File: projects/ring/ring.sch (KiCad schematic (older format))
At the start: 4 parts, among them U1 STM32WB55CEU6TR, Y1 NX1612SA-32.000MHZ-CHP-CIS-3

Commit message: layout and schem changes
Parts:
- removed E1: NN02-101, step-footprints:XCVR_NN02-101, symbol step:NN02-101
- added C1, C10, C11, C2, C5, C6, C8: C_100nF, Capacitor_SMD:C_0402_1005Metric, symbol step:C_100nF
- added C7, C9: C_4.7uF, Capacitor_SMD:C_01005_0402Metric, symbol step:C_4.7uF
- added L1: L_10uH_LQM21FN100M70L, Inductor_SMD:L_0805_2012Metric, symbol step:L_10uH_LQM21FN100M70L
- added L2: L_10nH_LQG15WZ10NJ02D, Inductor_SMD:L_0402_1005Metric, symbol step:L_10nH_LQG15WZ10NJ02D
- added TP1, TP2, TP3, TP4, TP5: Test_Point_SMD, footprints:Test_Point_SMD, symbol step:Test_Point_SMD
- added U2: LSM6DSO32TR, step-footprints:LSM6DSO32TR, symbol step:LSM6DSO32TR
- added U3: ANT016008LCS2442MA2, step-footprints:ANT016008LCS2442MA2, symbol step:ANT016008LCS2442MA2
- added U4: BQ297xy, Package_SON:WSON-6_1.5x1.5mm_P0.5mm, symbol Battery_Management:BQ297xy
- Y1: footprint OSCSC105P160X120X35-4N -> step-footprints:OSCSC105P160X120X35-4N
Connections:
- net labels added: +BATT, BOOT0, CS, LSM_INT1, LSM_INT2, MISO, MOSI, SCK, SWCLK, SWDIO, rad_plane
- wire segments 11 -> 45
- no-connect marks 0 -> 6
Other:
- note added: "Accelerometer"
- note added: "Can be connected to any STM GPIO \nand used to wake from sleep mode \nvia the EXTI Interrupt"
- note added: "Inductors for \nOn-Die SMPS"
- note added: "Integrated Passive Device \nMatching, PI, LP Filter"
- note added: "SMD Chip Antenna"
- note added: "STM smps"
- note added: "fets @sam"
- note added: "power net"
- note added: "should be vreg"
- moved on the sheet: Y1

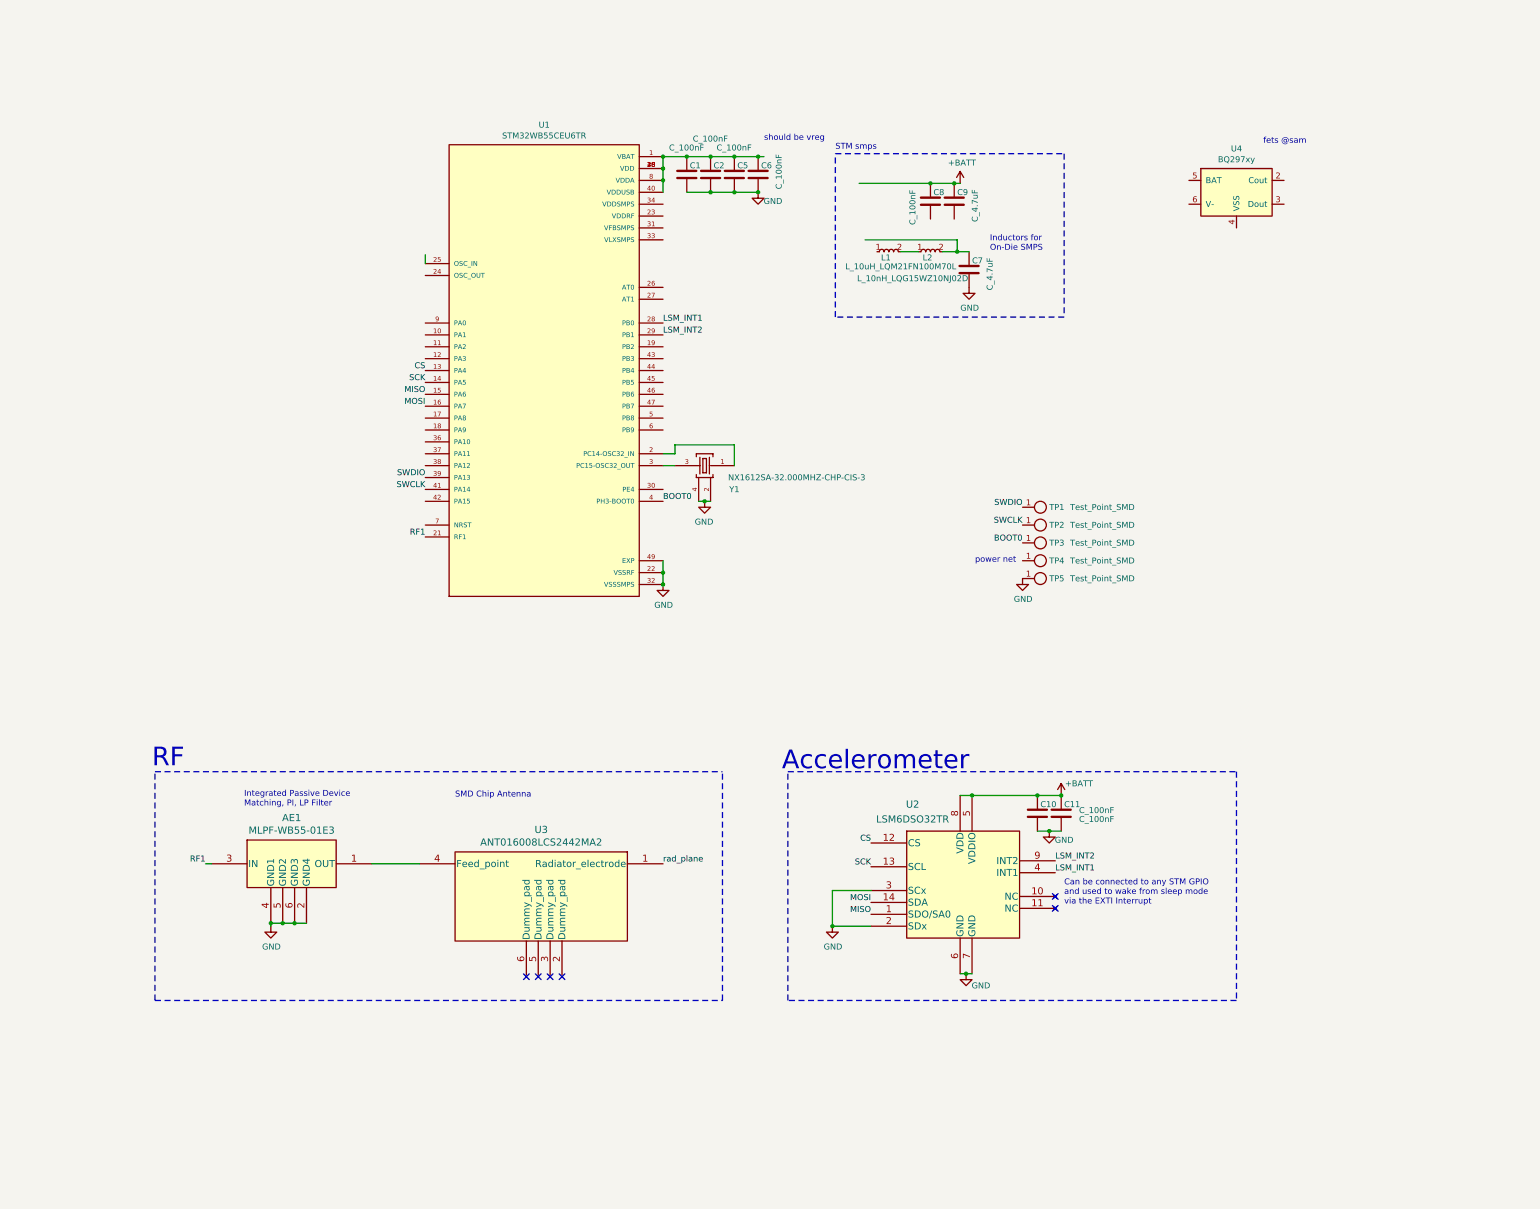
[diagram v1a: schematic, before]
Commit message: ring hardware schem & layout updates
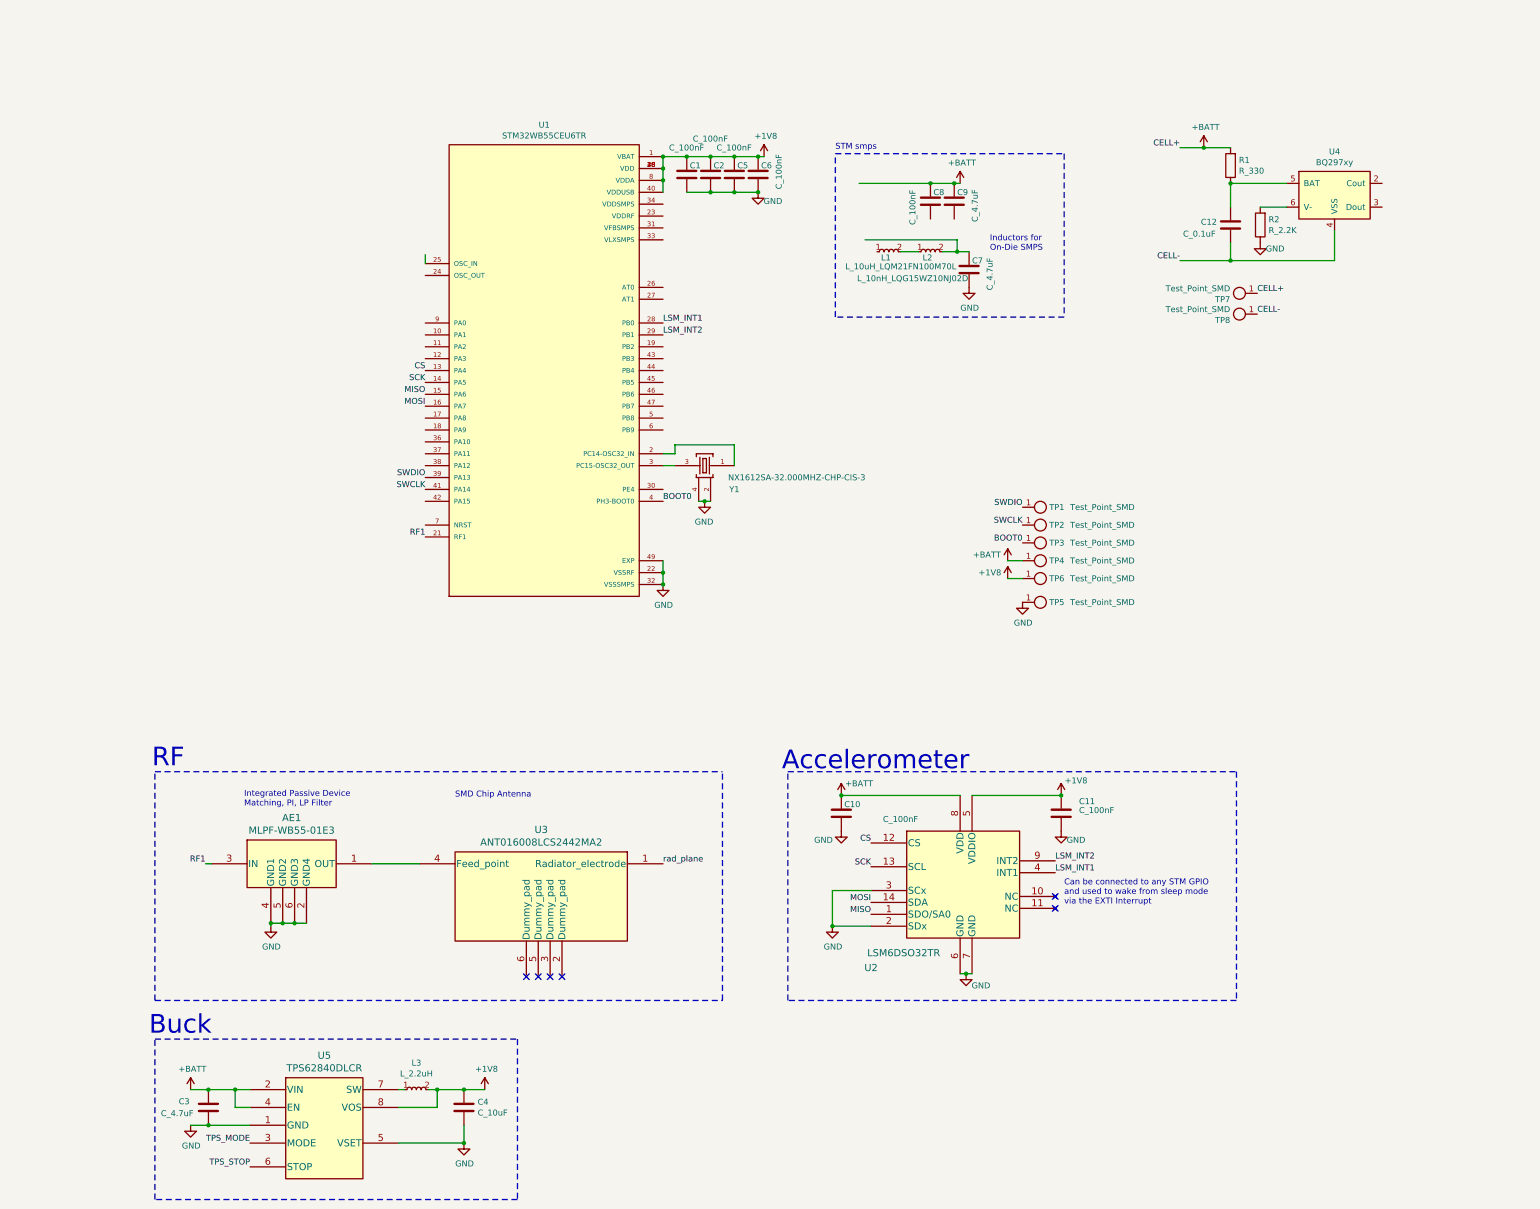
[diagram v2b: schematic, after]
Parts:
- added C12: C_0.1uF, footprints:C_0805_OEM, symbol step:C_0.1uF
- added C3: C_4.7uF, Capacitor_SMD:C_0402_1005Metric, symbol step:C_4.7uF
- added C4: C_10uF, Capacitor_SMD:C_0402_1005Metric, symbol step:C_10uF
- added L3: L_2.2uH, Inductor_SMD:L_0805_2012Metric_Pad1.05x1.20mm_HandSolder, symbol step:L_2.2uH
- added R1: R_330, Resistor_SMD:R_0402_1005Metric, symbol step:R_330
- added R2: R_2.2K, Resistor_SMD:R_0402_1005Metric, symbol step:R_2.2K
- added TP6: Test_Point_SMD, TestPoint:TestPoint_Pad_1.0x1.0mm, symbol step:Test_Point_SMD
- added TP7, TP8: Test_Point_SMD, footprints:Test_Point_SMD, symbol step:Test_Point_SMD
- added U5: TPS62840DLCR, step-footprints:TPS62840DLCR, symbol step:TPS62840DLCR
- C7, C9: footprint Capacitor_SMD:C_01005_0402Metric -> Capacitor_SMD:C_0402_1005Metric
- TP1, TP2, TP3, TP4, TP5: footprint footprints:Test_Point_SMD -> TestPoint:TestPoint_Pad_1.0x1.0mm
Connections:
- net labels added: +1V8, CELL+, CELL-, TPS_MODE, TPS_STOP
- wire segments 45 -> 68
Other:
- note added: "Buck"
- note removed: "fets @sam"
- note removed: "power net"
- note removed: "should be vreg"
- moved on the sheet: C10, TP5, U4

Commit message: nearly complete first pass schem, RF ready for review
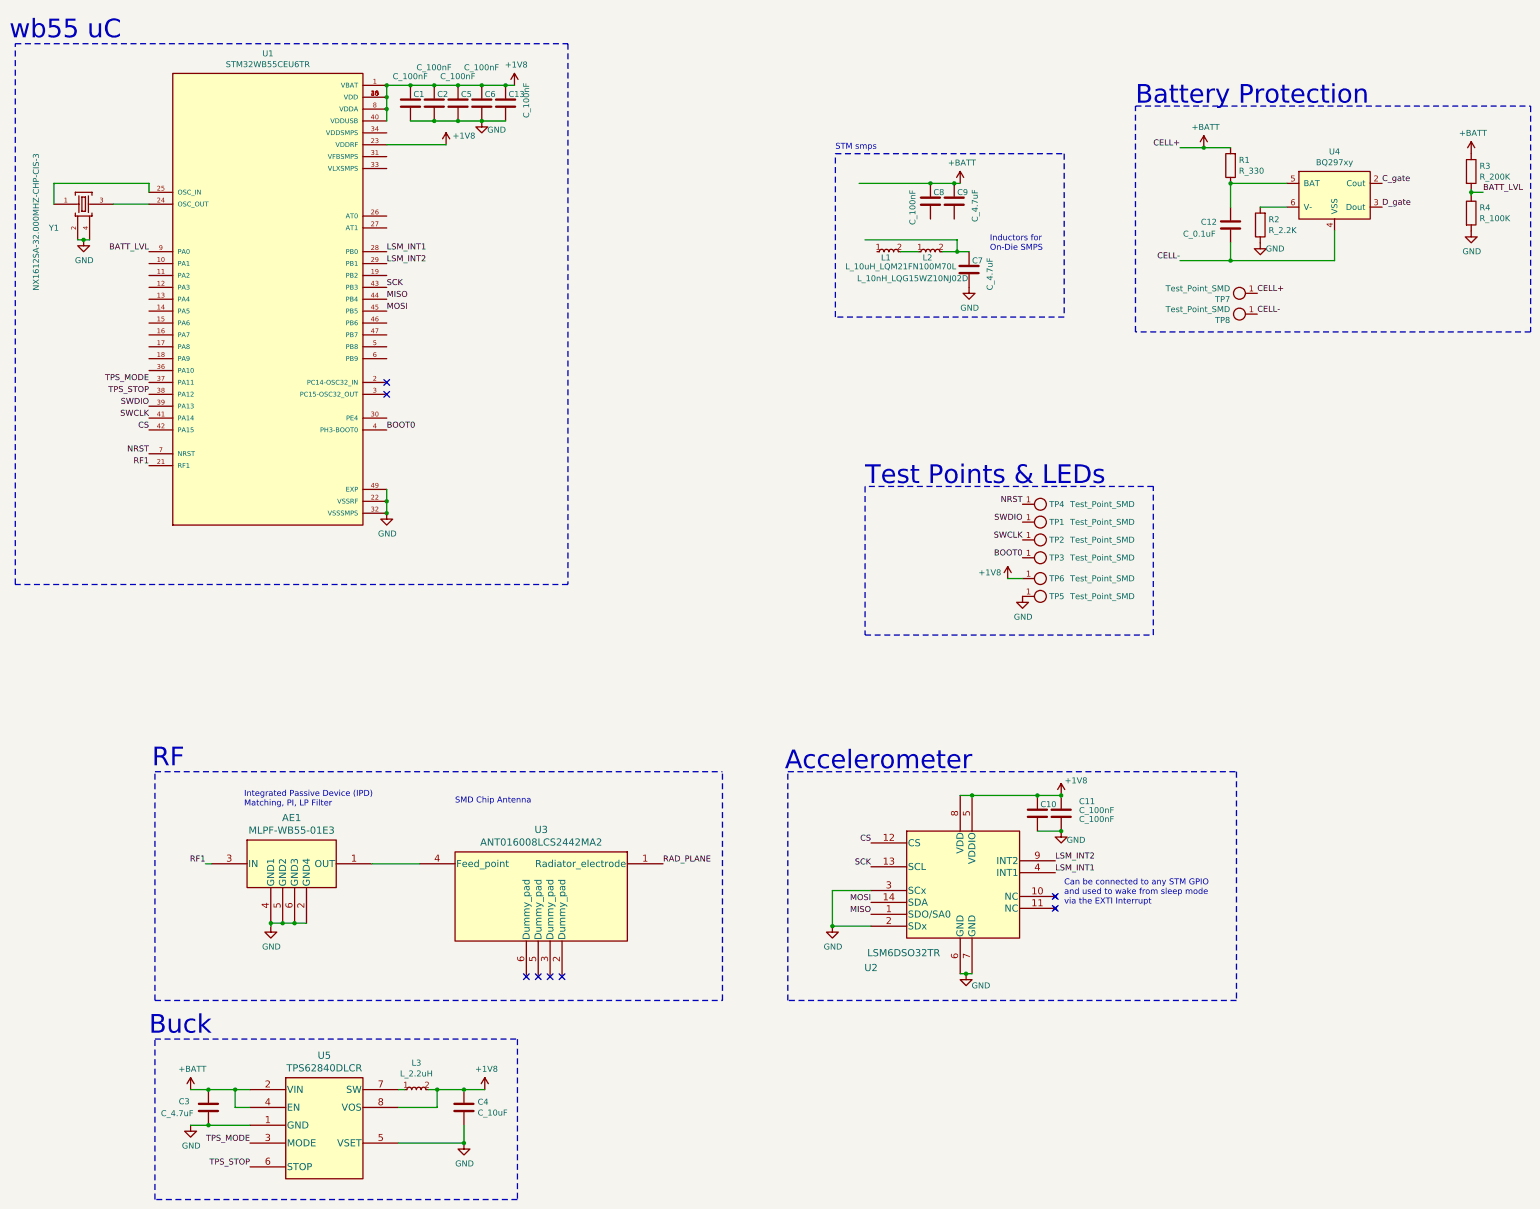
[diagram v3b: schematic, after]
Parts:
- added C13: C_100nF, Capacitor_SMD:C_0402_1005Metric, symbol step:C_100nF
- added R3: R_200K, Resistor_SMD:R_0402_1005Metric, symbol step:R_200K
- added R4: R_100K, Resistor_SMD:R_0402_1005Metric, symbol step:R_100K
- C12: footprint footprints:C_0805_OEM -> Capacitor_SMD:C_0402_1005Metric
- TP7, TP8: footprint footprints:Test_Point_SMD -> TestPoint:TestPoint_Pad_2.0x2.0mm
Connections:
- net labels added: BATT_LVL, C_gate, D_gate, NRST, RAD_PLANE
- net labels removed: rad_plane
- wire segments 68 -> 73
- no-connect marks 6 -> 8
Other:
- note added: "Battery Protection"
- note added: "Integrated Passive Device (IPD)\nMatching, PI, LP Filter"
- note added: "Test Points & LEDs"
- note added: "wb55 uC"
- note removed: "Integrated Passive Device \nMatching, PI, LP Filter"
- moved on the sheet: C1, C10, C2, C5, C6, TP1, TP2, TP3, TP5, U1, Y1

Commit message: an inch closer to hardware first rev completion
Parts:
- removed C7, C9: C_4.7uF, Capacitor_SMD:C_0402_1005Metric, symbol step:C_4.7uF
- removed C8: C_100nF, Capacitor_SMD:C_0402_1005Metric, symbol step:C_100nF
- removed L1: L_10uH_LQM21FN100M70L, Inductor_SMD:L_0805_2012Metric, symbol step:L_10uH_LQM21FN100M70L
- removed L2: L_10nH_LQG15WZ10NJ02D, Inductor_SMD:L_0402_1005Metric, symbol step:L_10nH_LQG15WZ10NJ02D
- added D1: LED_Amber, LED_SMD:LED_0402_1005Metric, symbol step:LED_0805_Amber
- added Q1, Q2: CSD17318Q2T, step-footprints:TRANS_CSD17318Q2T, symbol step:CSD17318Q2T
- added R5: R_1K, Resistor_SMD:R_0402_1005Metric, symbol step:R_1K
- added TP10, TP11, TP12, TP13, TP9: Test_Point_SMD, TestPoint:TestPoint_Pad_1.0x1.0mm, symbol step:Test_Point_SMD
- AE1: buy (none) -> https://www.digikey.com/en/products/detail/stmicroelectroni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
- TP7, TP8: footprint TestPoint:TestPoint_Pad_2.0x2.0mm -> TestPoint:TestPoint_Pad_1.5x1.5mm
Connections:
- net +1V8: now also U1.31 (VFBSMPS), U1.33 (VLXSMPS), U1.34 (VDDSMPS), TP13.1
- net CELL-: now also Q1.4, Q1.7
- net C_gate: now also Q2.3
- net D_gate: now also Q1.3
- net GND: now also Q2.4, Q2.7, R5.2
- net BTN_0: now reaches U1.13 (PA4)
- net BTN_0: now also TP9.1
- net BTN_1: now reaches U1.14 (PA5)
- net BTN_1: now also TP10.1
- net BTN_2: now reaches U1.15 (PA6)
- net BTN_2: now also TP11.1
- net BTN_3: now reaches U1.16 (PA7)
- net BTN_3: now also TP12.1
- net LED_1: now reaches U1.6 (PB9)
- net LED_1: now also D1.2 (A)
- new net: D1.1 (K), R5.1
- new net DRAIN: Q1.1, Q1.2, Q1.5, Q1.6, Q1.8, Q2.1, Q2.2, Q2.5, Q2.6, Q2.8
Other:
- note added: "1/3 Resistor Divider \nto uC ADC"
- note added: "32MHz External \nclk; required for RF"
- note added: "4x Button TP's - \nSolder N/O Button \nbetween 1V8 & it's pad"
- note added: "Backside LED\nfor testing to DNP"
- note added: "Battery Terminal\nSolder Pads\n"
- note added: "Button Pads"
- note added: "Low side shared drain \nNMOS Load Switch \n"
- note added: "System Power (Buck)"
- note added: "Wired for internal LDO \nconfig; see pg 27"
- note removed: "Buck"
- note removed: "Inductors for \nOn-Die SMPS"
- note removed: "STM smps"
- moved on the sheet: AE1, C10, C11, C12, C3, C4, L3, R1, R2, R3, R4, TP1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

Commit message: int2, silkscreen, DRC DRC DRC FUCK
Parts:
- removed Q1, Q2: CSD17318Q2T, step-footprints:TRANS_CSD17318Q2T, symbol step:CSD17318Q2T
- added Q1: AOCA32116E, step-footprints:AOCA32116E, symbol step:AOCA32116E
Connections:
- net +BATT: now also TP8.1; no longer TP7.1
- net CELL-: now also TP7.1, Q1.1 (S); no longer TP8.1
- net C_gate: now also Q1.3 (G)
- net D_gate: now also Q1.4 (G)
- net GND: now also Q1.2 (S)
- net LSM_INT1: now also U1.12 (PA3); no longer U1.28 (PB0)
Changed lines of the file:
@@
 	1    0    0    -1
 $EndComp
-Text Label 3800 2575 0    50   ~ 0
+Text Label 1800 2875 2    50   ~ 0
 LSM_INT1
 Text Label 3800 2675 0    50   ~ 0
@@
 	0    -1   -1   0
 $EndComp
+Text Label 6400 2575 0    50   ~ 0
+CELL+
 Text Label 6400 2400 0    50   ~ 0
-CELL+
-Text Label 6400 2575 0    50   ~ 0
 CELL-
 Connection ~ 6350 1475
@@
 32MHz External \nclk; required for RF
 Connection ~ 4800 1475
-$Comp
-L step:CSD17318Q2T Q1
-U 1 1 625AFF6F
-P 7875 2125
-F 0 "Q1" V 8027 2171 50  0000 L CNN
-F 1 "CSD17318Q2T" V 8125 1725 50  0000 L CNN
-F 2 "step-footprints:TRANS_CSD17318Q2T" H 8025 2125 50  0001 L BNN
-F 3 "https://www.ti.com/general/docs/suppproductinfo.tsp?distId=10&gotoUrl=https%3A%2F%2Fwww.ti.com%2Flit%2Fgpn%2Fcsd17318q2" H 7875 2125 50  0001 L BNN
-F 4 "https://www.digikey.com/en/products/detail/texas-instruments/CSD17318Q2T/7596430" H 9675 2075 50  0001 C CNN "buy"
-	1    7875 2125
-	0    1    1    0
-$EndComp
-$Comp
-L step:CSD17318Q2T Q2
-U 1 1 625BBCD7
-P 8275 2125
-F 0 "Q2" V 8427 2171 50  0000 L CNN
-F 1 "CSD17318Q2T" V 8525 1750 50  0000 L CNN
-F 2 "step-footprints:TRANS_CSD17318Q2T" H 8425 2125 50  0001 L BNN
-F 3 "https://www.ti.com/general/docs/suppproductinfo.tsp?distId=10&gotoUrl=https%3A%2F%2Fwww.ti.com%2Flit%2Fgpn%2Fcsd17318q2" H 8275 2125 50  0001 L BNN
-F 4 "https://www.digikey.com/en/products/detail/texas-instruments/CSD17318Q2T/7596430" H 10075 2075 50  0001 C CNN "buy"
-	1    8275 2125
-	0    -1   1    0
-$EndComp
-Wire Wire Line
-	7675 2125 7225 2125
-Connection ~ 7225 2125
-Wire Wire Line
-	7625 1675 7775 1675
-Wire Wire Line
-	7775 1675 7775 1825
-Wire Wire Line
-	7625 1475 8375 1475
-Wire Wire Line
-	8375 1475 8375 1825
+Wire Wire Line
+	7625 1675 7975 1675
+Wire Wire Line
+	7975 1675 7975 1825
+Wire Wire Line
+	7625 1475 8275 1475
+Wire Wire Line
+	8275 1475 8275 1825
 Wire Wire Line
 	8475 2125 8675 2125
@@
 Text Notes 6675 2600 0    50   ~ 0
 Battery Terminal\nSolder Pads\n
-Wire Wire Line
-	8075 2125 8075 1950
-Connection ~ 8075 2125
-Text Label 8075 1950 0    50   ~ 0
-DRAIN
 $Comp
 L step:LED_0805_Amber D1
@@
 Text Label 1800 3275 2    50   ~ 0
 BTN_3
+$Comp
+L step:AOCA32116E Q1
+U 1 1 6259FF6A
+P 8275 2125
+F 0 "Q1" V 8544 2275 50  0000 C CNN
+F 1 "AOCA32116E" V 8425 1800 50  0000 C CNN
+F 2 "step-footprints:AOCA32116E" H 8275 2125 50  0001 C CNN
+F 3 "http://www.aosmd.com/res/data_sheets/AOCA32116E.pdf" H 8275 2125 50  0001 C CNN
+F 4 "https://www.digikey.com/en/products/detail/alpha-omega-semiconductor-inc/AOCA32116E/12180390" H 8275 2125 50  0001 C CNN "buy"
+	1    8275 2125
+	0    -1   1    0
+$EndComp
+Wire Wire Line
+	7775 2125 7225 2125
+Connection ~ 7225 2125
 $EndSCHEMATC

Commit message: ready for first review
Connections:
- no-connect marks 8 -> 21
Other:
- note added: "Backside LED\nfor testing | DNP"
- note removed: "Backside LED\nfor testing to DNP"
- moved on the sheet: AE1, C10, C11, C3, C4, L3, U2, U3, U5
